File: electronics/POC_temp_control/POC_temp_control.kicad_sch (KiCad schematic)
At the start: 51 parts, among them J1 Conn_01x02, J2 Conn_01x07, Q1 PXT8050, Q2 PXT8050, Q3 PXT8550, T1 10P_1P_2S, U1 SY8120, U2 MCP1702T-3302

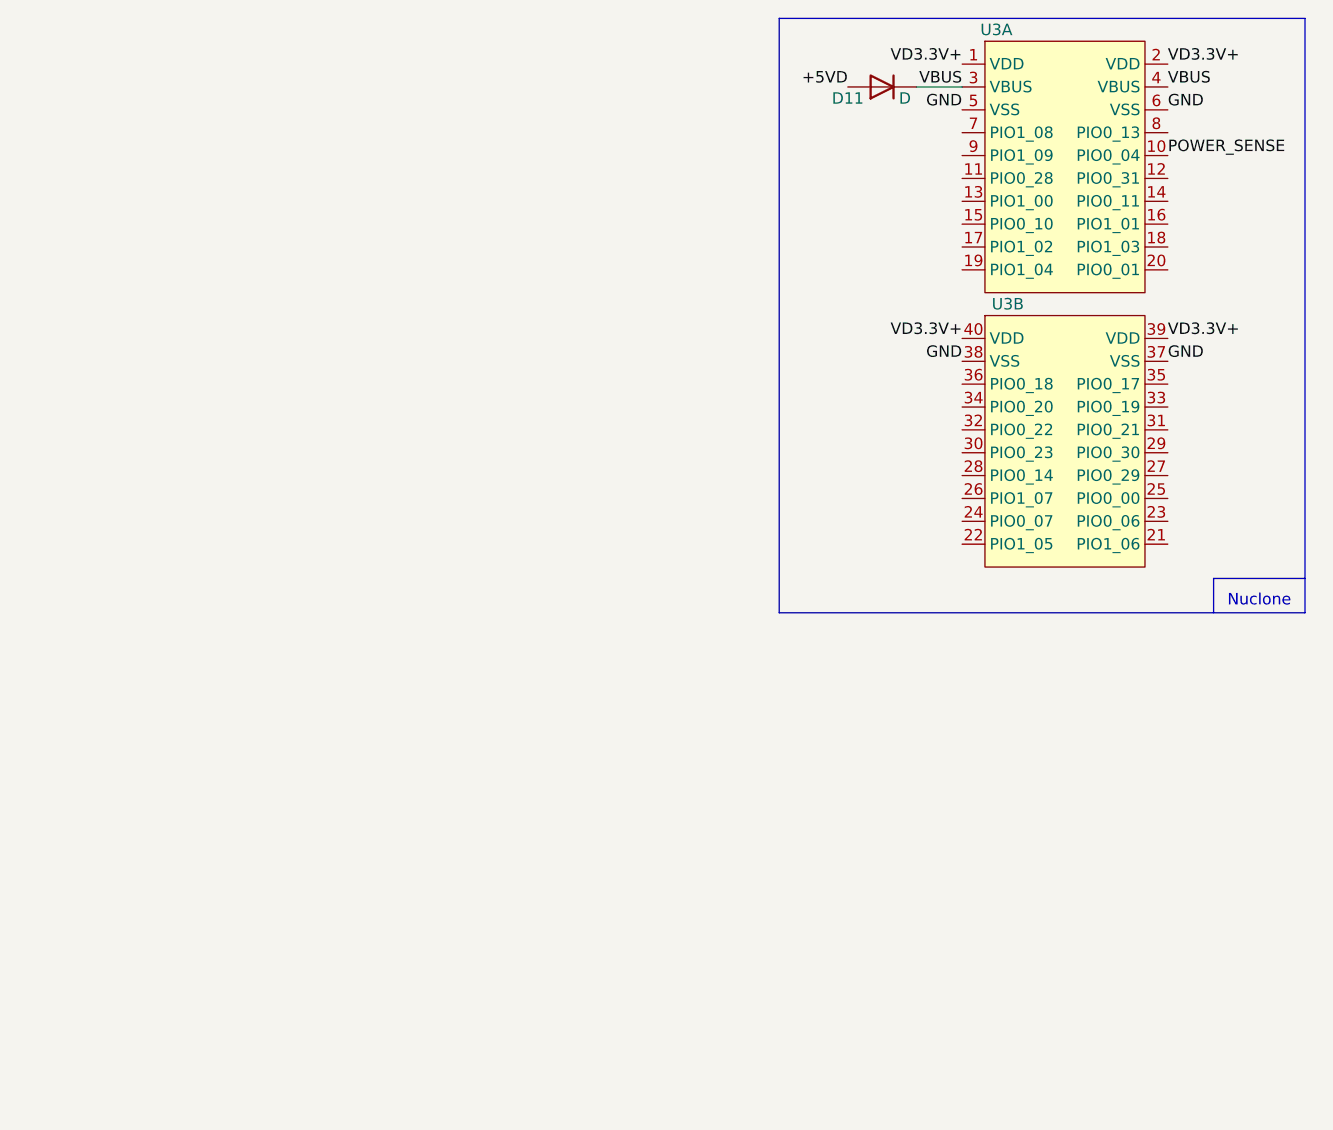
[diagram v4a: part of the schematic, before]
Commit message: analog input filtering and post amps, started with diff amps
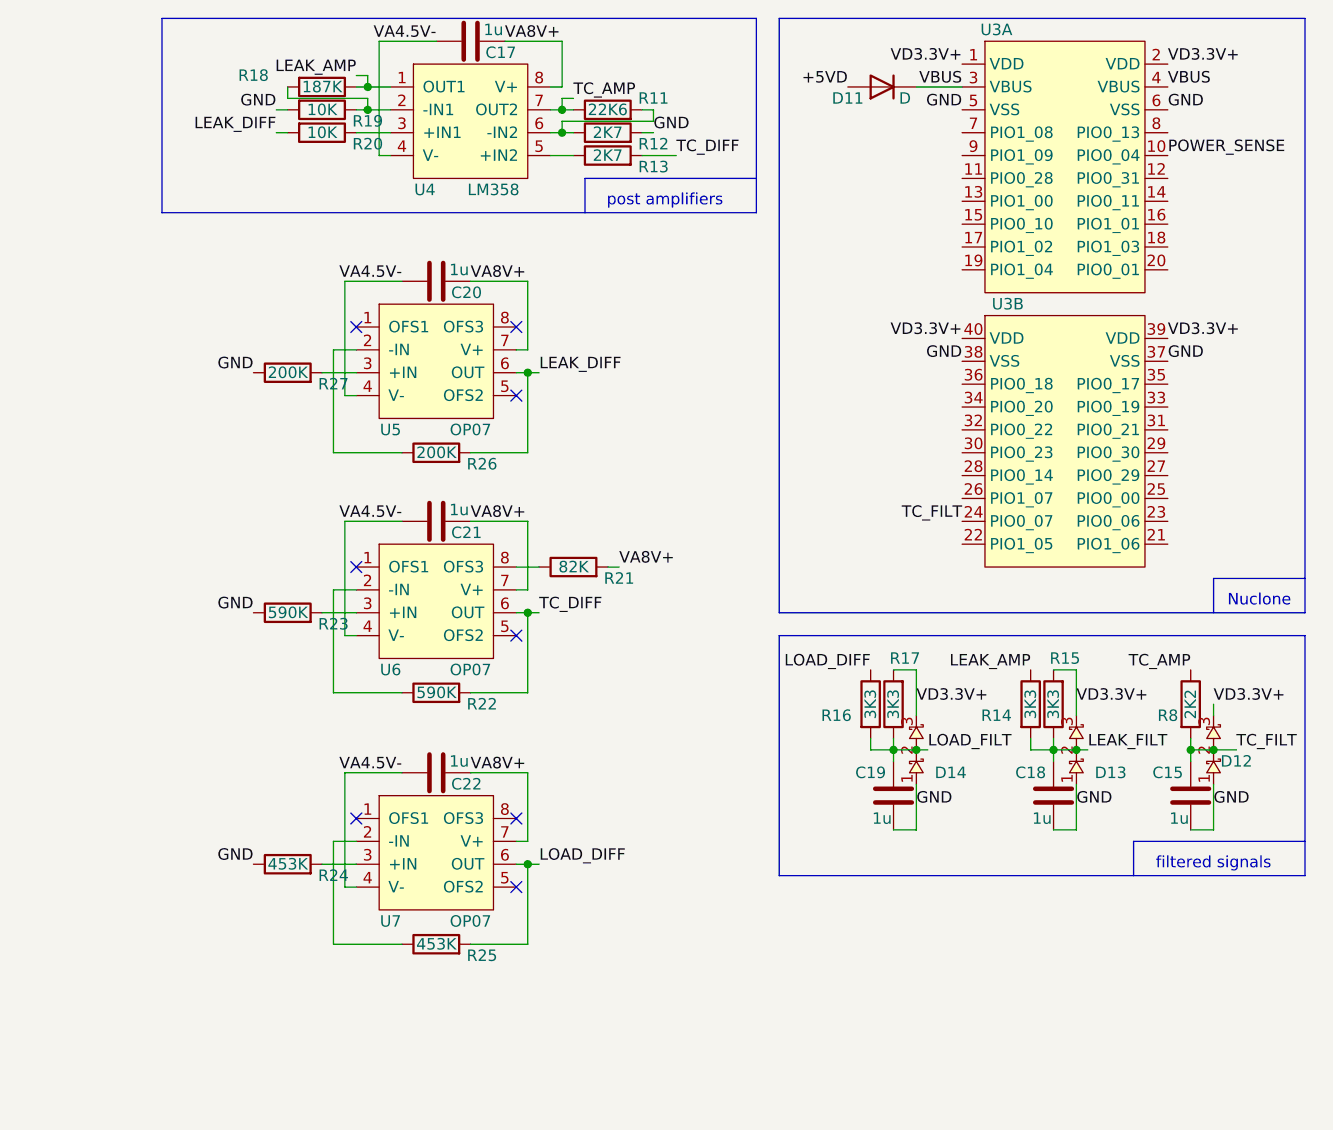
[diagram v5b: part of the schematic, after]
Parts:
- added C15, C18, C19: 1u, SquantorCapacitor:C_0805+0603, symbol Device:C
- added C17, C20, C21, C22: 1u, SquantorCapacitor:C_0603, symbol Device:C
- added D12, D13, D14: ~, SquantorIC:SOT23-3, symbol SquantorDiodes:shottky_series
- added R11: 22K6, SquantorResistor:R_0603_hand, symbol Device:R
- added R12, R13: 2K7, SquantorResistor:R_0603_hand, symbol Device:R
- added R14, R15, R16, R17: 3K3, SquantorResistor:R_0603_hand, symbol Device:R
- added R18: 187K, SquantorResistor:R_0603_hand, symbol Device:R
- added R19, R20: 10K, SquantorResistor:R_0603_hand, symbol Device:R
- added R21: 82K, SquantorResistor:R_0603_hand, symbol Device:R
- added R22, R23: 590K, SquantorResistor:R_0603_hand, symbol Device:R
- added R24, R25: 453K, SquantorResistor:R_0603_hand, symbol Device:R
- added R26, R27: 200K, SquantorResistor:R_0603_hand, symbol Device:R
- added R8: 2K2, SquantorResistor:R_0603_hand, symbol Device:R
- added U4: LM358, SquantorIC:SOIC-8, symbol SquantorGenericAnalog:opamp_dual_8pin
- added U5, U6, U7: OP07, SquantorIC:SOIC-8, symbol SquantorGenericAnalog:opamp_single_8pin
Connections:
- net GND: now also C15.2, C18.2, C19.2, D12.1, D13.1, D14.1, R12.2, R19.2, R23.1, R24.1, R27.1
- net VA4.5V-: now also C17.1, C20.1, C21.1, C22.1, U4.4 (V-), U5.4 (V-), U6.4 (V-), U7.4 (V-)
- net VA8V+: now also C17.2, C20.2, C21.2, C22.2, R21.2, U4.8 (V+), U5.7 (V+), U6.7 (V+), U7.7 (V+)
- net VD3.3V+: now also D12.3, D13.3, D14.3, R15.2, R17.2
- net TC_FILT: now reaches U3.24 (PIO0_07)
- net TC_FILT: now also C15.1, D12.2, R8.2
- new net: R13.1, U4.5 (+IN2)
- new net: R23.2, U6.3 (+IN)
- new net: R18.2, R19.1, U4.2 (-IN1)
- new net: R20.1, U4.3 (+IN1)
- new net: R11.2, R12.1, U4.6 (-IN2)
- new net: R22.1, U6.2 (-IN)
- new net: R21.1, U6.8 (OFS3)
- new net: R27.2, U5.3 (+IN)
- new net: R24.2, U7.3 (+IN)
- new net: R26.1, U5.2 (-IN)
- new net: R25.1, U7.2 (-IN)
- new net LEAK_AMP: R14.1, R18.1, U4.1 (OUT1)
- new net LEAK_DIFF: R20.2, R26.2, U5.6 (OUT)
- new net LEAK_FILT: C18.1, D13.2, R14.2, R15.1
- new net LOAD_DIFF: R16.1, R25.2, U7.6 (OUT)
- new net LOAD_FILT: C19.1, D14.2, R16.2, R17.1
- new net TC_AMP: R11.1, R8.1, U4.7 (OUT2)
- new net TC_DIFF: R13.2, R22.2, U6.6 (OUT)
- no-connect marks 0 -> 8
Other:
- note added: "filtered signals"
- note added: "post amplifiers"

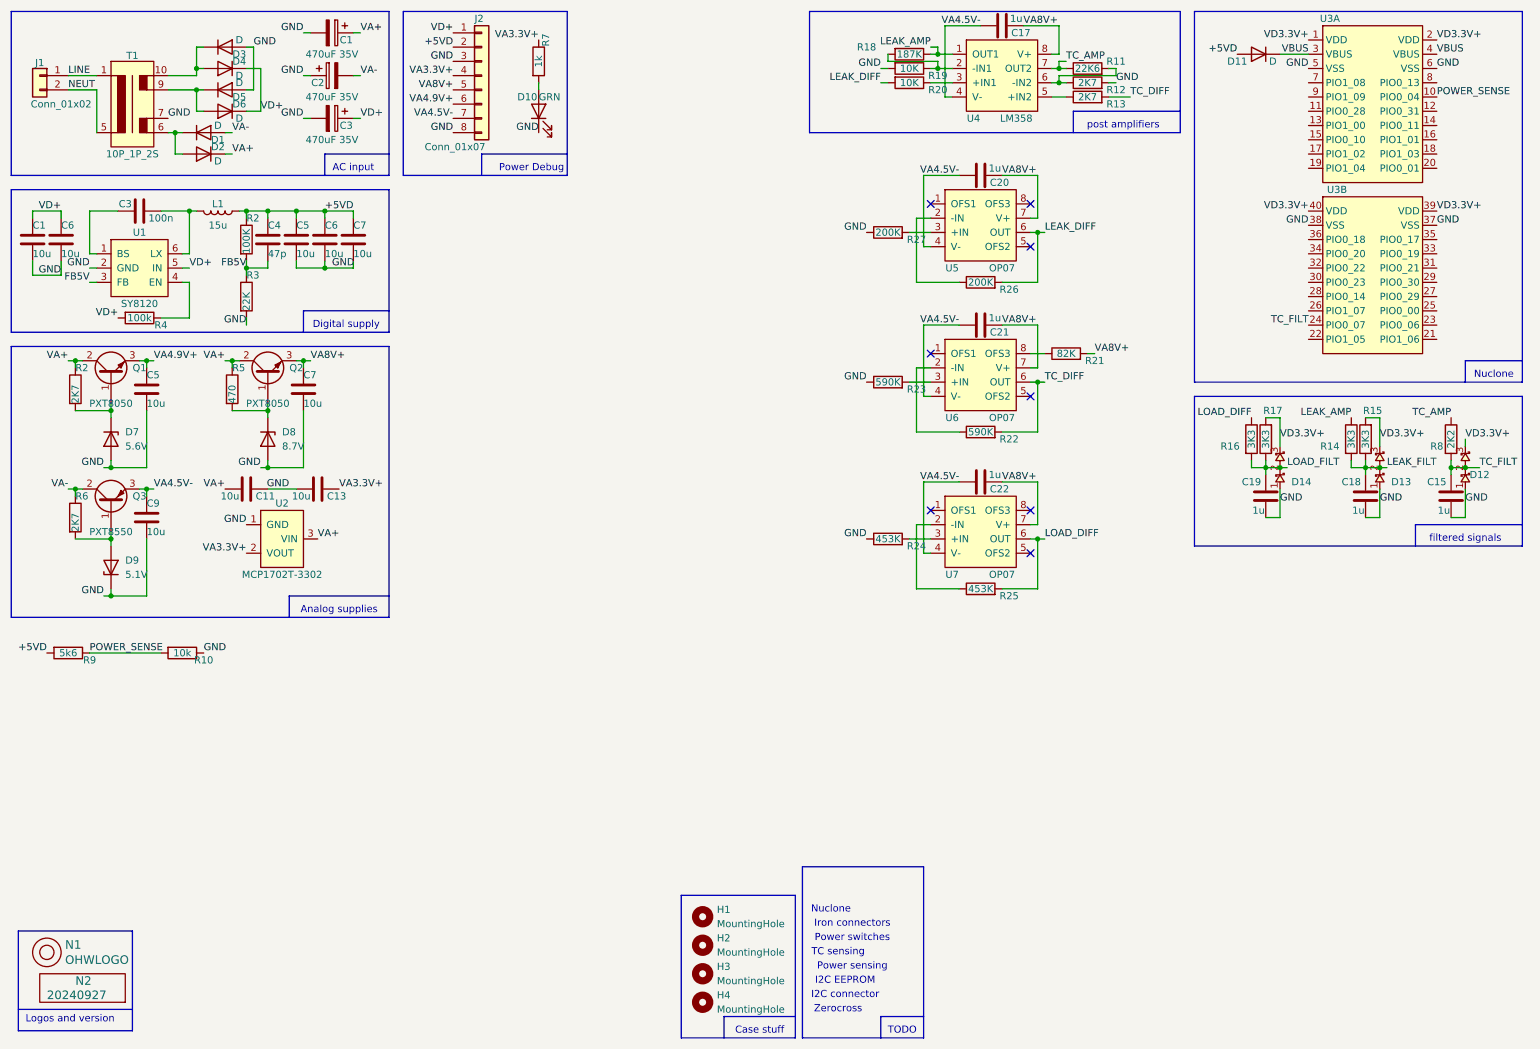
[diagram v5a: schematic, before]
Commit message: finished diff amp schematic and analog multiplexers
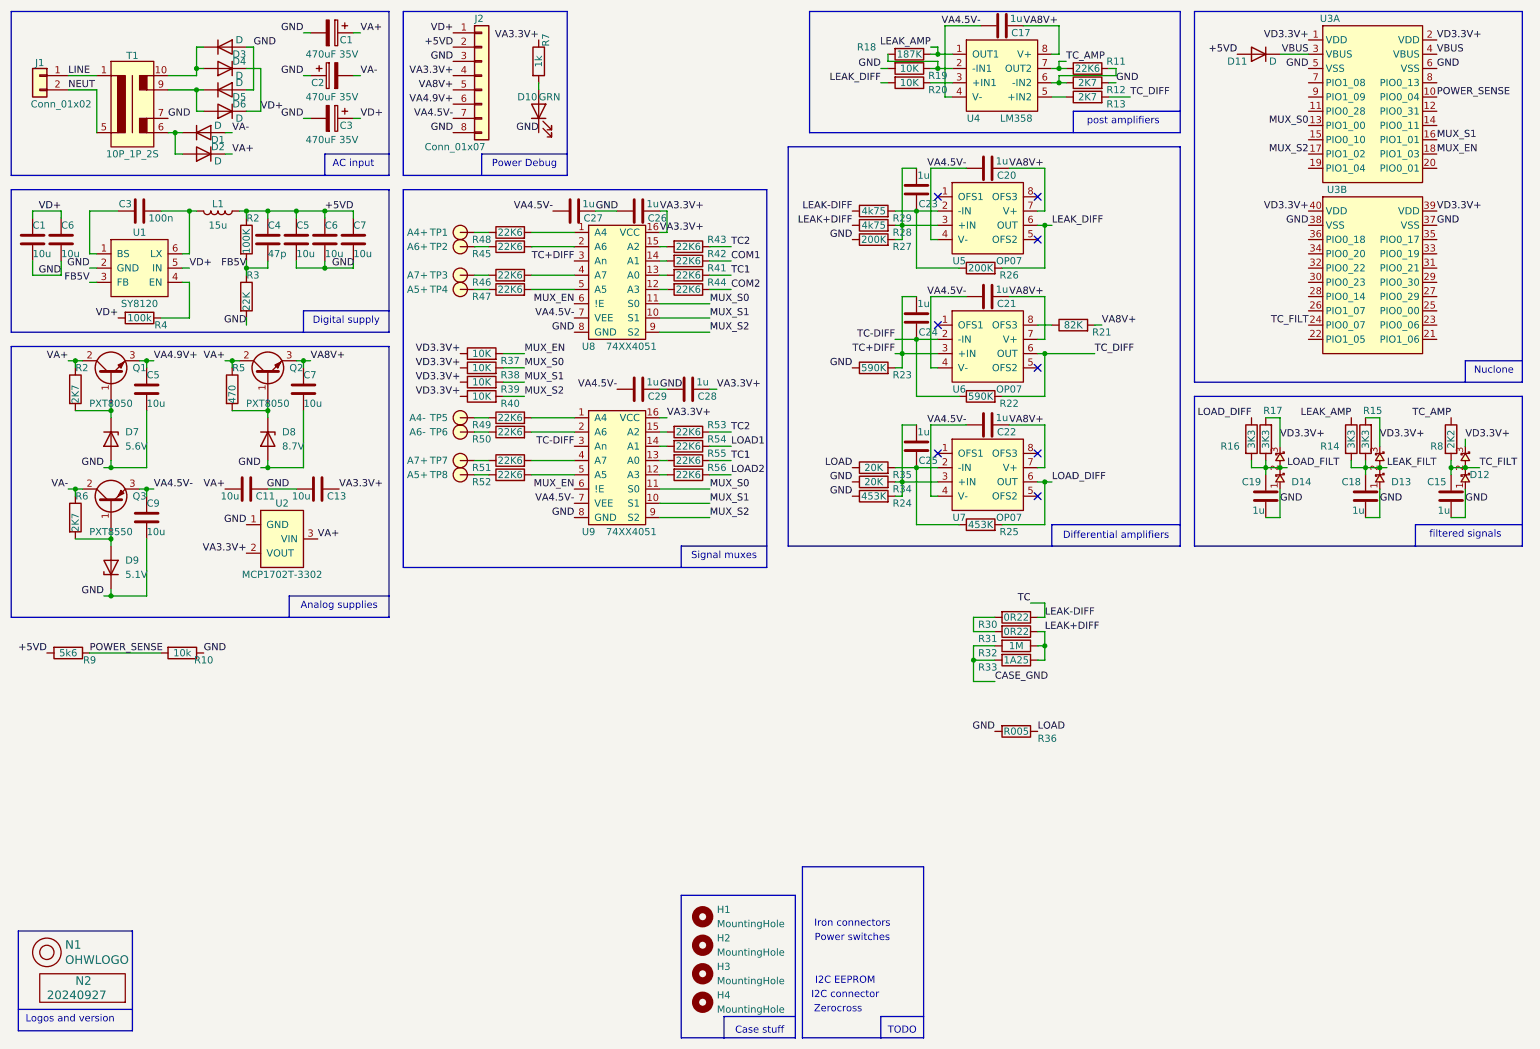
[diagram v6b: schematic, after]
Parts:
- added C23, C24, C25: 1u, SquantorCapacitor:C_0603, symbol Device:C
- added C26, C27, C28, C29: 1u, SquantorCapacitor:C_0805+0603, symbol Device:C
- added R28, R29: 4k75, SquantorResistor:R_0603_hand, symbol Device:R
- added R30, R31: 0R22, SquantorResistor:R_0805+0603, symbol Device:R
- added R32: 1M, SquantorResistor:R_1206, symbol Device:R
- added R33: 1A25, SquantorResistor:R_1206, symbol Device:R
- added R34, R35: 20K, SquantorResistor:R_0603_hand, symbol Device:R
- added R36: R005, SquantorResistor:R_2512, symbol Device:R
- added R37, R38, R39, R40: 10K, SquantorResistor:R_0603_hand, symbol Device:R
- added R41, R42, R43, R44, R45, R46, R47, R48, R49, R50, R51, R52, R53, R54, R55, R56: 22K6, SquantorResistor:R_0603_hand, symbol Device:R
- added TP1: A4+, SquantorTestPoints:TestPoint_hole_H03R07, symbol SquantorProto:testpad
- added TP2: A6+, SquantorTestPoints:TestPoint_hole_H03R07, symbol SquantorProto:testpad
- added TP3, TP7: A7+, SquantorTestPoints:TestPoint_hole_H03R07, symbol SquantorProto:testpad
- added TP4, TP8: A5+, SquantorTestPoints:TestPoint_hole_H03R07, symbol SquantorProto:testpad
- added TP5: A4-, SquantorTestPoints:TestPoint_hole_H03R07, symbol SquantorProto:testpad
- added TP6: A6-, SquantorTestPoints:TestPoint_hole_H03R07, symbol SquantorProto:testpad
- added U8, U9: 74XX4051, SquantorIC:SOIC-16_3.9x9.9mm_P1.27mm, symbol SquantorLogic:74XX4051
- C17, C20, C21, C22: footprint SquantorCapacitor:C_0603 -> SquantorCapacitor:C_0805+0603
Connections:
- net GND: now also C26.1, C27.2, C28.1, C29.2, R34.1, R36.2, U8.8 (GND), U9.8 (GND)
- net VA3.3V+: now also C26.2, C28.2, U8.16 (VCC), U9.16 (VCC)
- net VA4.5V-: now also C27.1, C29.1, U8.7 (VEE), U9.7 (VEE)
- net VD3.3V+: now also R37.1, R38.1, R39.1, R40.1
- net TC+DIFF: now reaches R23.2, U6.3 (+IN)
- net TC+DIFF: now also C24.2, U8.3 (An)
- net TC-DIFF: now reaches R22.1, U6.2 (-IN)
- net TC-DIFF: now also C24.1, U9.3 (An)
- net at R27.2, U5.3 (+IN): now also C23.2, R28.2
- net at R24.2, U7.3 (+IN): now also C25.2, R34.2
- net at R26.1, U5.2 (-IN): now also C23.1, R29.2
- net MUX_S0: now reaches U3.13 (PIO1_00)
- net MUX_S0: now also R38.2, U8.11 (S0), U9.11 (S0)
- net MUX_S1: now reaches U3.16 (PIO1_01)
- net MUX_S1: now also R39.2, U8.10 (S1), U9.10 (S1)
- net MUX_S2: now reaches U3.17 (PIO1_02)
- net MUX_S2: now also R40.2, U8.9 (S2), U9.9 (S2)
- net MUX_EN: now reaches U3.18 (PIO1_03)
- net MUX_EN: now also R37.2, U8.6 (!E), U9.6 (!E)
- net at R25.1, U7.2 (-IN): now also C25.1, R35.2
- new net: R49.1, TP5.1
- new net: R48.1, TP1.1
- new net: R52.1, TP8.1
- new net: R52.2, U9.5 (A5)
- new net: R41.2, U8.13 (A0)
- new net: R30.2, R31.2
- new net: R45.1, TP2.1
- new net: R42.2, U8.14 (A1)
- new net: R45.2, U8.2 (A6)
- new net: R55.2, U9.13 (A0)
- new net: R47.1, TP4.1
- new net: R44.2, U8.12 (A3)
- new net: R47.2, U8.5 (A5)
- new net: R46.1, TP3.1
- new net: R46.2, U8.4 (A7)
- new net: R54.2, U9.14 (A1)
- new net: R48.2, U8.1 (A4)
- new net: R50.1, TP6.1
- new net: R53.2, U9.15 (A2)
- new net: R51.1, TP7.1
- new net: R43.2, U8.15 (A2)
- new net: R50.2, U9.2 (A6)
- new net: R56.2, U9.12 (A3)
- new net: R51.2, U9.4 (A7)
- new net: R49.2, U9.1 (A4)
- new net CASE_GND: R32.2, R33.2
- new net COM1: R42.1
- new net COM2: R44.1
- new net LEAK+DIFF: R28.1, R31.1, R32.1, R33.1
- new net LEAK-DIFF: R29.1, R30.1
- new net LOAD: R35.1, R36.1
- new net LOAD1: R54.1
- new net LOAD2: R56.1
- new net TC1: R41.1, R55.1
- new net TC2: R43.1, R53.1
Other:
- note added: "Differential amplifiers"
- note added: "Signal muxes"
- note removed: "Power sensing"
- note removed: "TC sensing"
- moved on the sheet: C20, C21, C22, R21, R22, R23, R24, R25, R26, R27, U5, U6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

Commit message: WIP DIY soldering station
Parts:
- added C30: 1u, SquantorCapacitor:C_0805+0603, symbol Device:C
- added D17: BZX84C18, SquantorIC:SOT23-3, symbol SquantorDevice:D_Zener_Small_A1C3
- added D18: BAS16, SquantorIC:SOT23-3, symbol SquantorDevice:D_Small_A1C3
- added D19: BAV79, SquantorIC:SOT23-3, symbol SquantorDevice:D_CC_AAC
- added J3: Conn_01x05, Connector_JST:JST_XH_B5B-XH-A_1x05_P2.50mm_Vertical, symbol Connector_Generic:Conn_01x05
- added J4: Conn_01x06, Connector_JST:JST_XH_B6B-XH-A_1x06_P2.50mm_Vertical, symbol Connector_Generic:Conn_01x06
- added J5, J6: Conn_01x02, SquantorPhoenixContact:MKDS_2conn_508pitch_1711725, symbol Connector_Generic:Conn_01x02
- added JP1, JP2: AC, SquantorSpecial:solder_jumper_3mm_SMD, symbol SquantorSpecial:Solderjumper_2way_noconn
- added OP1, OP2: ~, SquantorOpto:OP_SOIC_4, symbol SquantorOpto:OP_Q_single
- added Q4: Q_PMOS_DUAL, SquantorIC:SOIC-8, symbol SquantorDevice:Q_PMOS_DUAL_8pin
- added Q5: BC858B, SquantorIC:SOT23-3, symbol Device:Q_PNP_BEC
- added Q6: BC847A, SquantorIC:SOT23-3, symbol Device:Q_NPN_BEC
- added R57: 10M, SquantorResistor:R_0603_hand, symbol Device:R
- added R58: 5K6, SquantorResistor:R_0603_hand, symbol Device:R
- added R59: 1M, SquantorResistor:R_0603_hand, symbol Device:R
- added R60: 2K2, SquantorResistor:R_0603_hand, symbol Device:R
- added R61: 1K5, SquantorResistor:R_0603_hand, symbol Device:R
- added R62, R63: 330, SquantorResistor:R_0603_hand, symbol Device:R
- added R64, R65, R66: 10K, SquantorResistor:R_0603_hand, symbol Device:R
- added R67: 6K8, SquantorResistor:R_0603_hand, symbol Device:R
- C26, C27, C28, C29: footprint SquantorCapacitor:C_0805+0603 -> SquantorCapacitor:C_0603
- F1: renamed from R33; symbol Device:R -> Device:Fuse
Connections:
- net COM1: now also J4.2 (Pin_2), Q4.3 (S2), R57.2
- net COM2: now also J3.2 (Pin_2)
- net GND: now also D18.1 (A), J6.2 (Pin_2), Q6.2 (E), R62.1
- net LOAD1: now also J4.5 (Pin_5)
- net LOAD2: now also J3.3 (Pin_3)
- net TC1: now also J4.1 (Pin_1)
- net TC2: now also J3.1 (Pin_1)
- net VD3.3V+: now also Q5.2 (E), R63.2, R65.2, R67.2
- new net: OP2.1, R63.1
- new net: OP2.2, Q6.3 (C)
- new net: D19.2 (K2), OP2.4, R58.2, R61.2
- new net: C30.1, D17.3 (K), OP1.4, R60.1
- new net: D18.3 (K), R60.2
- new net: Q5.1 (B), R64.1, R67.1
- new net: OP1.1, Q5.3 (C)
- new net: Q6.1 (B), R66.1
- new net: OP1.3, R61.1
- new net: OP1.2, R62.2
- new net AC1: J5.2 (Pin_2), J6.1 (Pin_1), JP2.1
- new net AC2: J5.1 (Pin_1), JP1.1
- new net AC_P1: JP1.2, JP2.2, Q4.1 (S1), R57.1
- new net SW_GATE_1: D19.3 (K1A2), Q4.2 (G1), Q4.4 (G2), R58.1, R59.1
- new net SW_LOAD_1: R64.2, R65.1, R66.2
- new net SW_SRC_1: C30.2, D17.1 (A), D19.1 (A1), OP2.3, Q4.5 (D2), Q4.6 (D2), Q4.7 (D1), Q4.8 (D1), R59.2
- no-connect marks 8 -> 13
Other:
- note added: "Iron connections"
- note added: "Power in"
- moved on the sheet: C11, C13, C5, C7, C9, D7, D8, D9, Q1, Q2, Q3, R10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
